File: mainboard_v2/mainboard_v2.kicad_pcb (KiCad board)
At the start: 4 copper layers, 68 x 86.5 mm, 80 parts, among them J1 Servo, J2 Buzzer, J4 Button Interface, J5 Power, J6 Release Button, J7 Extra Pins, Q1 BSS138, Q2 BSS138, Q3 BSS138, Q4 BSS138, Q5 BSS138, Q6 BSS138, SW1 SW_Push, U1 RP2040, U2 W25Q128JVS, U3 RV-3028-C7, U4 ITR9608-F, U5 TCA9535RTWR, U6 11405, Y1 Crystal_ABM8

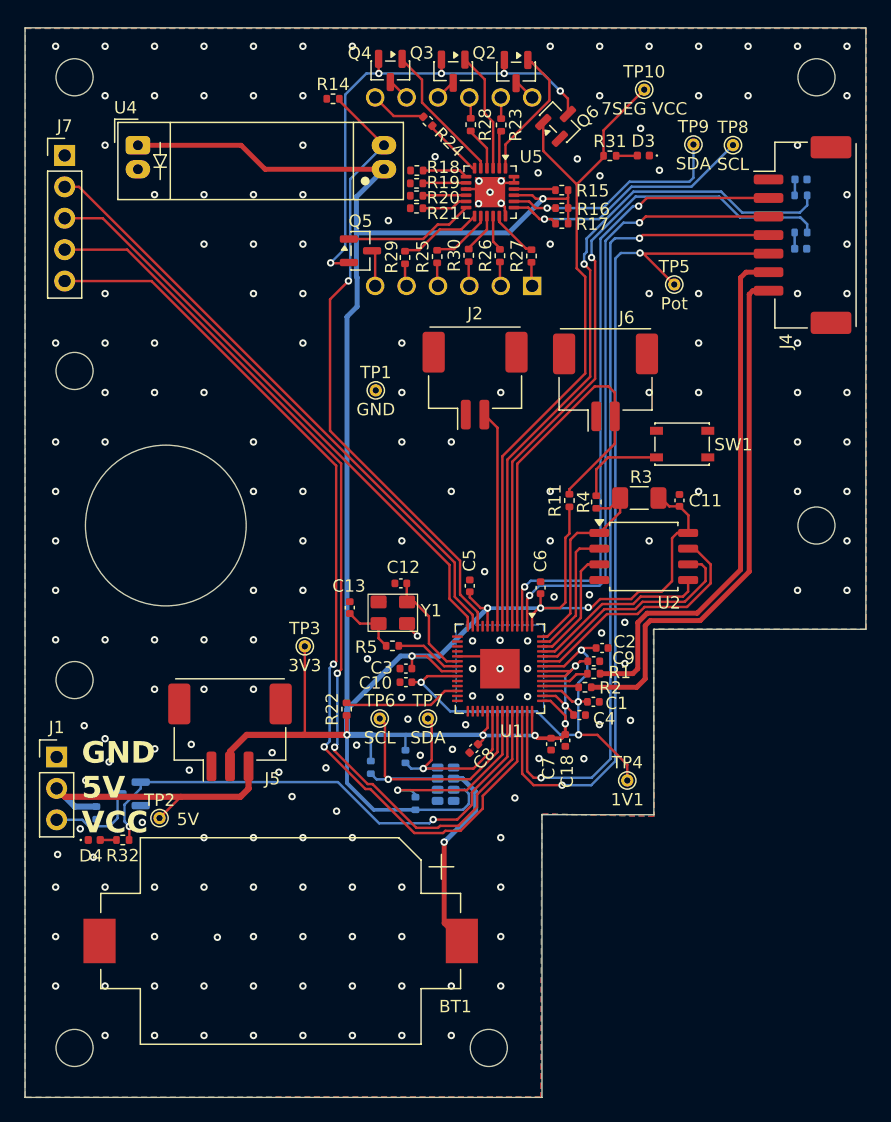
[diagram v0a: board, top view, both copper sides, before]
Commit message: updated MCU from RP2040 to ATmega328p
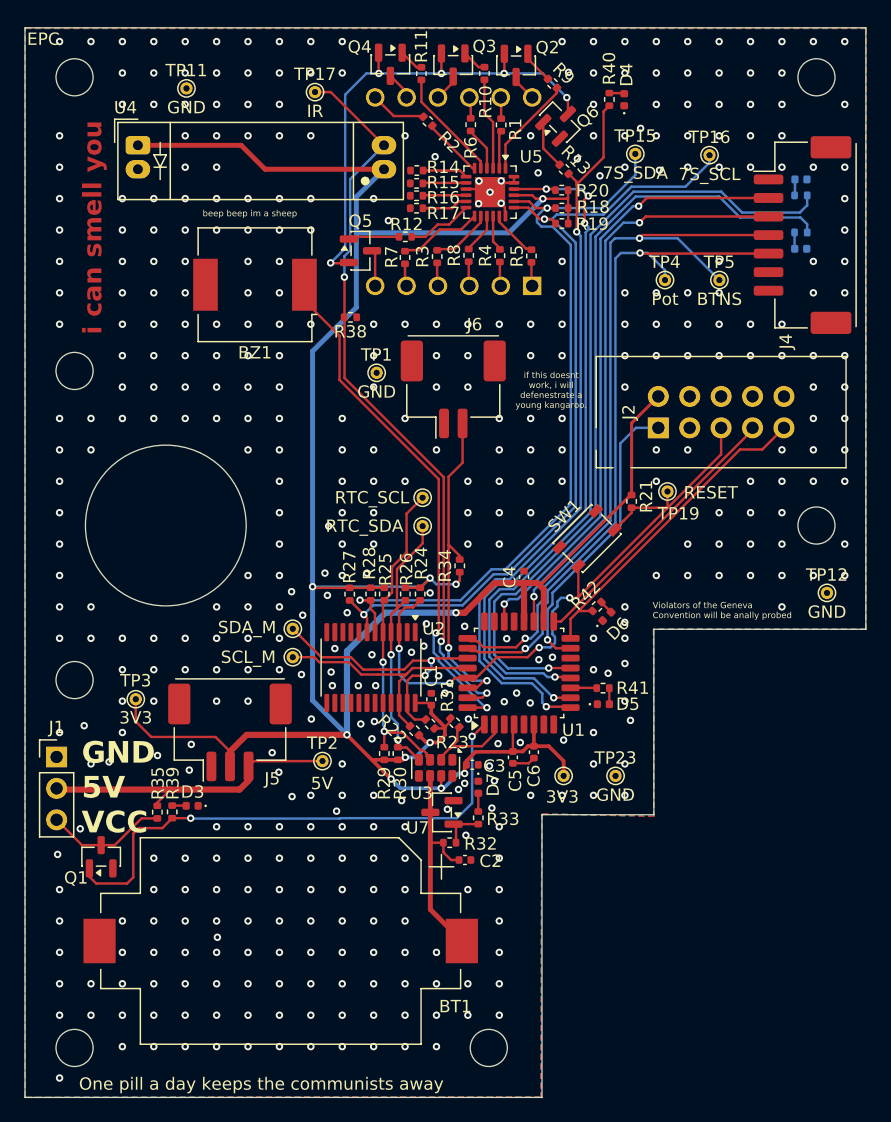
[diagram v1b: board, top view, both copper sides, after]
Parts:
- removed C10, C11, C18, C7, C8, C9: 100n, Capacitor_SMD:C_0402_1005Metric
- removed C12, C13: 15p, Capacitor_SMD:C_0402_1005Metric
- removed J7: Extra Pins, Connector_PinHeader_2.54mm:PinHeader_1x05_P2.54mm_Vertical
- removed the R1 at (123.7, 109.7)
- removed the R2 at (123.0, 110.8)
- removed the R3 at (127.4, 95.5)
- removed the R31 at (125.0, 67.8)
- removed the R4 at (123.9, 95.8)
- removed the R5 at (107.5, 107.5)
- removed TP10: 7SEG VCC, TestPoint:TestPoint_THTPad_D1.0mm_Drill0.5mm
- removed TP8: SCL, TestPoint:TestPoint_THTPad_D1.0mm_Drill0.5mm
- removed TP9: SDA, TestPoint:TestPoint_THTPad_D1.0mm_Drill0.5mm
- removed Y1: Crystal_ABM8, Crystal:ABM8
- added BZ1: Buzzer, Buzzer_Beeper:Buzzer_CUI_CPT-9019S-SMT, F.Cu at (96.3, 78.3)
- added D5: LED, LED_SMD:LED_0402_1005Metric, F.Cu at (124.5, 112.2)
- added D6: LED, LED_SMD:LED_0402_1005Metric, F.Cu at (124.8, 105.1)
- added D7: LED, LED_SMD:LED_0402_1005Metric, F.Cu at (114.4, 118.9)
- added R10: 100, Resistor_SMD:R_0402_1005Metric, F.Cu at (114.9, 61.2)
- added R11: 100, Resistor_SMD:R_0402_1005Metric, F.Cu at (109.8, 61.2)
- added R12: 100, Resistor_SMD:R_0402_1005Metric, F.Cu at (108.5, 74.4)
- added R13: 100, Resistor_SMD:R_0402_1005Metric, F.Cu at (121.3, 68.9)
- added R21: 10k, Resistor_SMD:R_0402_1005Metric, F.Cu at (126.8, 95.8)
- added R23: 4.7k, Resistor_SMD:R_0402_1005Metric, F.Cu at (110.5, 113.8)
- added R24: 4.7k, Resistor_SMD:R_0402_1005Metric, F.Cu at (109.7, 103.3)
- added R25: 4.7k, Resistor_SMD:R_0402_1005Metric, F.Cu at (106.8, 103.3)
- added R26: 4.7k, Resistor_SMD:R_0402_1005Metric, F.Cu at (108.5, 103.3)
- added R27: 4.7k, Resistor_SMD:R_0402_1005Metric, F.Cu at (104.0, 103.3)
- added R28: 4.7k, Resistor_SMD:R_0402_1005Metric, F.Cu at (105.7, 103.3)
- added R33: 100, Resistor_SMD:R_0402_1005Metric, F.Cu at (114.4, 121.4)
- added R39: 1k, Resistor_SMD:R_0402_1005Metric, F.Cu at (89.6, 120.9)
- added R40: 1k, Resistor_SMD:R_0402_1005Metric, F.Cu at (125.0, 63.3)
- added R41: 1k, Resistor_SMD:R_0402_1005Metric, F.Cu at (124.5, 110.9)
- added R42: 1k, Resistor_SMD:R_0402_1005Metric, F.Cu at (124.0, 104.3)
- added R9: 100, Resistor_SMD:R_0402_1005Metric, F.Cu at (120.4, 62.0)
- added TP11: GND, TestPoint:TestPoint_THTPad_D1.0mm_Drill0.5mm, F.Cu at (90.8, 62.4)
- added TP12: GND, TestPoint:TestPoint_THTPad_D1.0mm_Drill0.5mm, F.Cu at (142.6, 103.2)
- added TP13: RTC_SDA, TestPoint:TestPoint_THTPad_D1.0mm_Drill0.5mm, F.Cu at (109.9, 97.8)
- added TP14: RTC_SCL, TestPoint:TestPoint_THTPad_D1.0mm_Drill0.5mm, F.Cu at (109.9, 95.5)
- added TP15: 7S_SDA, TestPoint:TestPoint_THTPad_D1.0mm_Drill0.5mm, F.Cu at (127.1, 67.7)
- added TP16: 7S_SCL, TestPoint:TestPoint_THTPad_D1.0mm_Drill0.5mm, F.Cu at (133.1, 67.8)
- added TP17: IR, TestPoint:TestPoint_THTPad_D1.0mm_Drill0.5mm, F.Cu at (101.2, 62.7)
- added TP18: 3V3, TestPoint:TestPoint_THTPad_D1.0mm_Drill0.5mm, F.Cu at (121.3, 118.0)
- added TP19: RESET, TestPoint:TestPoint_THTPad_D1.0mm_Drill0.5mm, F.Cu at (129.7, 95.0)
- added TP23: GND, TestPoint:TestPoint_THTPad_D1.0mm_Drill0.5mm, F.Cu at (125.5, 118.0)
- added U7: APX803SR, Package_TO_SOT_SMD:SOT-23, F.Cu at (111.5, 121.0)
- C1, C4: value 1u -> 100nF
- C2, C3, C5, C6: value 100n -> 100nF
- J2: value Buzzer -> ISP Header; footprint Connector_Molex:Molex_CLIK-Mate_505405-0270_1x02-1MP_P1.50mm_Vertical -> Connector_PinHeader_2.54mm:SBH11-PBPC-05
- J4: value Button Interface -> HCI Board Conn.
- Q1, U3: moved to F.Cu
- R1: renamed from R23; value 200 -> 100
- R18: renamed from R16; value 10k -> 4.7k
- R19: renamed from R17; value 10k -> 4.7k
- R2: renamed from R24; value 200 -> 100
- R20: renamed from R15; value 10k -> 4.7k
- R22: value 10k -> 4.7k
- R29: renamed from R6; moved to F.Cu
- R3: renamed from R25; value 200 -> 100
- R30: renamed from R7; moved to F.Cu
- R31: renamed from R8; moved to F.Cu
- R32: value 220 -> 100k
- R35: renamed from R13; moved to F.Cu
- R36: renamed from R9; value 220 -> 200
- R37: renamed from R10; value 220 -> 200
- R4: renamed from R26; value 200 -> 100
- R5: renamed from R27; value 200 -> 100
- R6: renamed from R28; value 200 -> 100
- R7: renamed from R29; value 200 -> 100
- R8: renamed from R30; value 200 -> 100
- TP4: value 1V1 -> Pot
- TP5: value Pot -> BTNS
- TP6: value SCL -> SDA_M
- TP7: value SDA -> SCL_M
- U1: value RP2040 -> ATmega328P-A; footprint Package_DFN_QFN:QFN-56-1EP_7x7mm_P0.4mm_EP3.2x3.2mm -> Package_QFP:TQFP-32_7x7mm_P0.8mm
- U2: value W25Q128JVS -> TCA9548APWR; footprint Package_SO:SOIC-8_5.3x5.3mm_P1.27mm -> Package_SO:TSSOP-24_4.4x7.8mm_P0.65mm
- U4: value ITR9608-F -> EE-SX1140
- U6: value 11405 -> LDQ-N514RI
- moved D4 73.6 mm to (126.2, 63.3), turned to 90 degrees
- moved D3 64.0 mm to (91.3, 120.4)
- moved TP4 40.6 mm to (129.5, 77.9)
- moved R32 26.4 mm to (112.1, 123.4)
- moved U2 23.8 mm to (105.7, 109.2), turned to -90 degrees
- moved C2 20.4 mm to (113.3, 124.8)
- moved R38 17.7 mm to (104.1, 80.9), turned to 180 degrees
- moved J2 15.3 mm to (129.0, 89.8), turned to 90 degrees
- moved TP3 14.3 mm to (86.7, 111.8)
- moved C5 14.3 mm to (117.2, 116.5)
- moved TP2 14.0 mm to (101.8, 116.8)
- moved C6 13.3 mm to (118.9, 116.1)
- moved C1 13.1 mm to (110.6, 111.8), turned to -90 degrees
- moved J6 12.3 mm to (112.4, 86.7)
- moved C4 12.0 mm to (118.1, 101.9), turned to 90 degrees
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- renumbered R18 to R14, R19 to R15, R20 to R16, R21 to R17, R11 to R34, R14 to R38
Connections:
- net /7-Segment/DP renamed DP
- net /7-Segment/LED_a renamed LED_a
- net /7-Segment/LED_b renamed LED_b
- net /7-Segment/LED_c renamed LED_c
- net /7-Segment/LED_d renamed LED_d
- net /7-Segment/LED_e renamed LED_e
- net /7-Segment/LED_f renamed LED_f
- net /7-Segment/LED_g renamed LED_g
- C1 pad 2: +1V1 -> AVCC
- C2 pad 2: +1V1 -> Net-(BT1-+)
- C3 pad 1: GND -> AVCC
- C3 pad 2: +1V1 -> GND
- C4 pad 1: GND -> AVCC
- C4 pad 2: +3.3V -> GND
- C5 pad 1: +3.3V -> GND
- C5 pad 2: GND -> AVCC
- C6 pad 1: +3.3V -> GND
- C6 pad 2: GND -> AVCC
- J2 pad 1: GND -> MOSI
- J2 pad 2: /Buzzer -> AVCC
- J4 pad 2: /AIN1 -> AIN1
- J4 pad 3: /AIN2 -> AIN2
- J4 pad 4: /BTNS -> BTNS
- J4 pad 5: /POT -> POT
- J4 pad 6: /USB D+ -> USB D+
- J4 pad 7: /USB D- -> USB D-
- J5 pad 2: +3.3V -> AVCC
- J6 pad 2: /B_RELEASE -> B_RELEASE
- Q1 pad 1: /SERVO_PWM -> SERVO_PWM
- Q2 pad 1: /7-Segment/CC1 -> Net-(Q2-G)
- Q3 pad 1: /7-Segment/CC2 -> Net-(Q3-G)
- Q4 pad 1: /7-Segment/CC3 -> Net-(Q4-G)
- Q5 pad 1: /7-Segment/CC4 -> Net-(Q5-G)
- Q6 pad 1: /7-SEG_PWM -> Net-(Q6-G)
- R18 pad 1: +3.3V -> AVCC
- R18 pad 2: /7-SEG_SDA -> 7-SEG_SDA
- R19 pad 1: +3.3V -> AVCC
- R19 pad 2: /7-SEG_SCL -> 7-SEG_SCL
- R20 pad 1: +3.3V -> AVCC
- R20 pad 2: Net-(U5-~{INT}) -> 7-SEG_INT
- R22 pad 1: +3.3V -> SCL_MASTER
- R22 pad 2: Net-(U1-RUN) -> AVCC
- R29 pad 1: +3.3V -> AVCC
- R29 pad 2: /RTC_SCL -> RTC_SCL
- R30 pad 1: +3.3V -> AVCC
- R30 pad 2: /RTC_SDA -> RTC_SDA
- R31 pad 1: +3.3V -> AVCC
- R31 pad 2: /RTC_INT -> RTC_INT
- R32 pad 1: Net-(D4-A) -> Net-(BT1-+)
- R32 pad 2: /SERVO_PWM -> Net-(U7-~{RST})
- R34 pad 1: +3.3V -> AVCC
- R34 pad 2: /B_RELEASE -> B_RELEASE
- R35 pad 1: +5V -> Net-(J1-Pin_3)
- R35 pad 2: unconnected-(R13-Pad2) -> +5V
- R36 pad 1: /WHITE_LED -> WHITE_LED
- R37 pad 1: /RED_LED -> RED_LED
- R38 pad 2: /IR -> IR
- SW1 pad 1: Net-(R4-Pad1) -> GND
- SW1 pad 2: GND -> RESET
- TP3 pad 1: +3.3V -> AVCC
- TP4 pad 1: +1V1 -> POT
- TP5 pad 1: /POT -> BTNS
- TP6 pad 1: /RTC_SCL -> SDA_MASTER
- TP7 pad 1: /RTC_SDA -> SCL_MASTER
- U1 pad 1: +3.3V -> SERVO_PWM
- U1 pad 10: +3.3V -> 7-SEG_INT
- U1 pad 11: unconnected-(U1-GPIO8-Pad11) -> POWER_LED
- U1 pad 12: /IR -> WHITE_LED
- U1 pad 13: /GPIO9 -> RED_LED
- U1 pad 14: /GPIO10 -> unconnected-(U1-PB2-Pad14)
- U1 pad 15: unconnected-(U1-GPIO12-Pad15) -> MOSI
- U1 pad 16: unconnected-(U1-GPIO13-Pad16) -> MISO
- U1 pad 17: unconnected-(U1-GPIO14-Pad17) -> SCK
- U1 pad 18: unconnected-(U1-GPIO15-Pad18) -> AVCC
- U1 pad 19: GND -> AIN2
- U1 pad 2: /AIN2 -> RTC_INT
- U1 pad 20: Net-(U1-XIN) -> AVCC
- U1 pad 21: Net-(U1-XOUT) -> GND
- U1 pad 22: +3.3V -> AIN1
- U1 pad 23: +1V1 -> unconnected-(U1-PC0-Pad23)
- U1 pad 25: unconnected-(U1-SWD-Pad25) -> BTNS
- U1 pad 26: Net-(U1-RUN) -> POT
- U1 pad 27: unconnected-(U1-GPIO16-Pad27) -> SDA_MASTER
- U1 pad 28: unconnected-(U1-GPIO17-Pad28) -> SCL_MASTER
- U1 pad 29: unconnected-(U1-GPIO18-Pad29) -> RESET
- U1 pad 3: /AIN1 -> GND
- U1 pad 30: unconnected-(U1-GPIO19-Pad30) -> B_RELEASE
- U1 pad 31: unconnected-(U1-GPIO20-Pad31) -> IR
- U1 pad 32: unconnected-(U1-GPIO21-Pad32) -> BUZZER
- U1 pad 4: /B_RELEASE -> AVCC
- U1 pad 5: /RED_LED -> GND
- U1 pad 6: /WHITE_LED -> AVCC
- U1 pad 7: /7-SEG_PWM -> unconnected-(U1-XTAL1/PB6-Pad7)
- U1 pad 8: /Buzzer -> unconnected-(U1-XTAL2/PB7-Pad8)
- U1 pad 9: unconnected-(U1-GPIO7-Pad9) -> 7-SEG_PWM
- U2 pad 1: /QSPI_SS -> GND
- U2 pad 2: /QSPI_SD1 -> GND
- U2 pad 3: /QSPI_SD2 -> RESET
- U2 pad 4: GND -> RTC_SDA
- U2 pad 5: /QSPI_SD0 -> RTC_SCL
- U2 pad 6: /QSPI_SCLK -> 7-SEG_SDA
- U2 pad 7: /QSPI_SD3 -> 7-SEG_SCL
- U2 pad 8: +3.3V -> unconnected-(U2-SD2-Pad8)
- U3 pad 2: /RTC_INT -> RTC_INT
- U3 pad 3: /RTC_SCL -> RTC_SCL
- U3 pad 4: /RTC_SDA -> RTC_SDA
- U3 pad 7: +3.3V -> AVCC
- U4 pad 1: +3.3V -> AVCC
- U4 pad 3: +3.3V -> AVCC
- U4 pad 4: /IR -> IR
- U5 pad 1: /7-Segment/CC1 -> CC1
- U5 pad 12: /7-Segment/CC4 -> CC4
- U5 pad 19: /7-SEG_SCL -> 7-SEG_SCL
- U5 pad 20: /7-SEG_SDA -> 7-SEG_SDA
- U5 pad 21: +3.3V -> AVCC
- U5 pad 22: Net-(U5-~{INT}) -> 7-SEG_INT
- U5 pad 3: /7-Segment/CC2 -> CC2
- U5 pad 5: /7-Segment/CC3 -> CC3
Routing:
- net +3.3V: track 238.2 -> 0.00 mm, vias 11 -> 0
- net AVCC: track 0.00 -> 232.0 mm, vias 0 -> 11
- net /GPIO27_ADC1: track 76.9 -> 0.00 mm, vias 2 -> 0
- net /GPIO26_ADC0: track 76.9 -> 0.00 mm, vias 2 -> 0
- net /POT: track 70.8 -> 0.00 mm, vias 2 -> 0
- net 7-SEG_SCL: track 0.00 -> 67.7 mm, vias 0 -> 2
- net /BTNS: track 67.2 -> 0.00 mm, vias 2 -> 0
- net WHITE_LED: track 0.00 -> 66.2 mm, vias 0 -> 1
- net RED_LED: track 0.00 -> 64.5 mm, vias 0 -> 1
- net 7-SEG_SDA: track 0.00 -> 63.4 mm, vias 0 -> 2
- net BTNS: track 0.00 -> 61.3 mm, vias 0 -> 2
- net 7-SEG_PWM: track 0.00 -> 60.7 mm, vias 0 -> 2
- net IR: track 0.00 -> 60.2 mm, vias 0 -> 3
- net 7-SEG_INT: track 0.00 -> 57.3 mm, vias 0 -> 4
- net POT: track 0.00 -> 55.8 mm, vias 0 -> 2
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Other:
- board text added: "EPC"
- board text added: "One pill a day keeps the communists away"
- board text added: "Violators of the Geneva Convention will be anally probed"
- board text added: "beep beep im a sheep"
- board text added: "chat am i cooked?"
- board text added: "i can smell you"
- board text added: "if this doesnt work, i will defenestrate a young kangaroo."
- board text added: "this project was powered by 54mg of Methylphenidate"

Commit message: final tweaks
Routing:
- net GND: vias 455 -> 214
